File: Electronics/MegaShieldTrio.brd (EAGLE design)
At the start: 99.8 x 80 mm, 40 parts, among them X1 Vehicle control, X2 ODO_JACK, X3 ODO_JACK, X4 RJ45-8L-B, X5 RJ45-8L-B

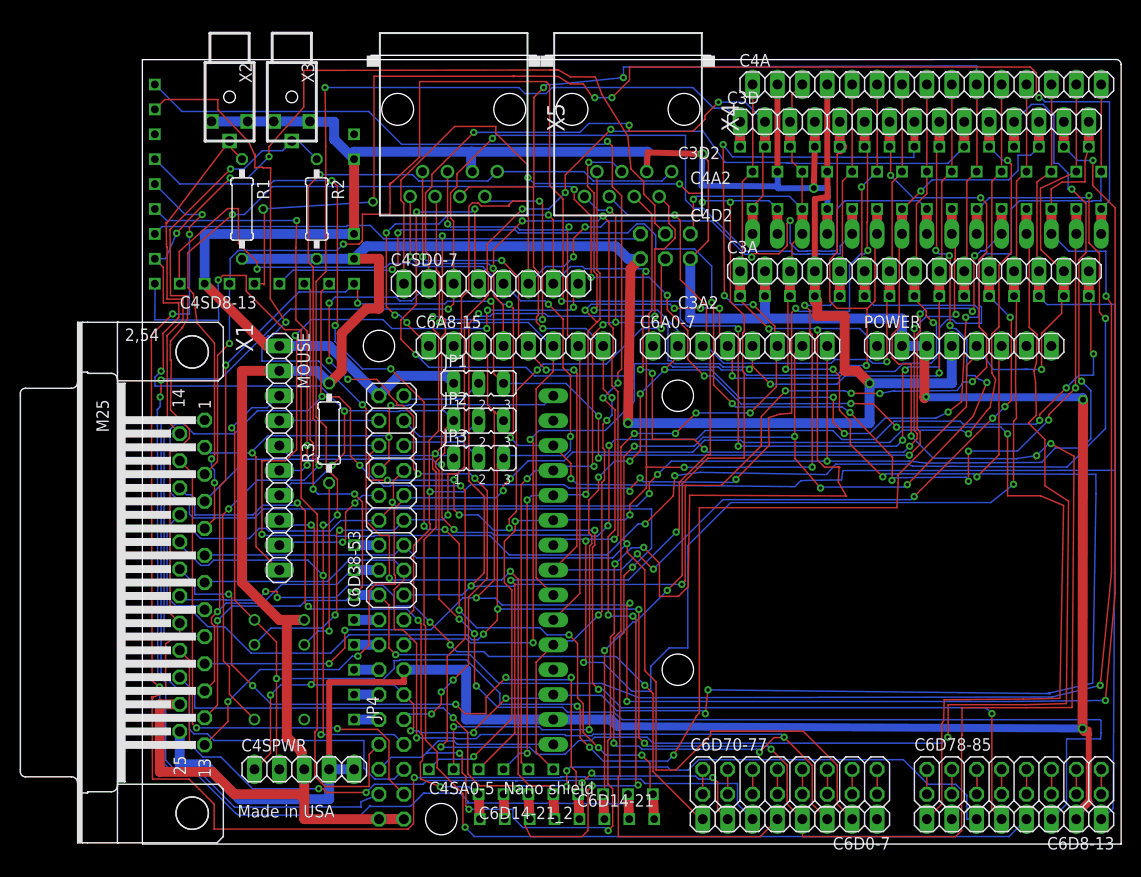
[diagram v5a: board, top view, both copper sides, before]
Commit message: Proto area; thickened traces
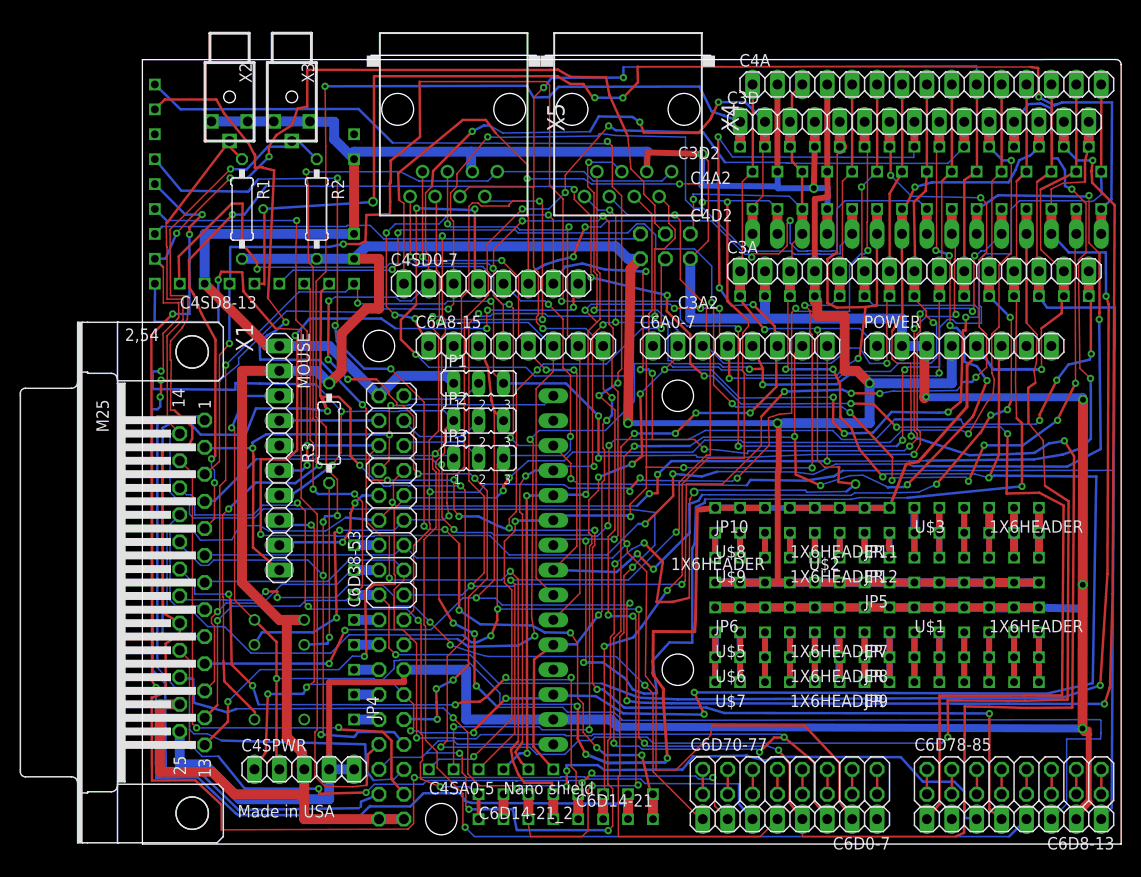
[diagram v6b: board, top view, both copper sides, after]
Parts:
- added JP10, JP11, JP12, JP5, JP6, JP7, JP8, JP9: (no value), Elcano:1X8HEADER
- added U$1, U$2, U$3, U$5, U$6, U$7, U$8, U$9: 1X6HEADER, Elcano:1X6HEADER
- moved C6D14-21 0.13 mm to (52.1, 2.54)
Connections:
- new net N$1: JP11.P$1, JP12.P$1
- new net N$10: JP11.P$3, JP12.P$3, U$3.P$1
- new net N$11: JP11.P$4, JP12.P$4, U$3.P$2
- new net N$12: JP11.P$5, JP12.P$5, U$3.P$3
- new net N$13: JP11.P$6, JP12.P$6, U$3.P$4
- new net N$14: JP11.P$7, JP12.P$7, U$3.P$5
- new net N$15: JP11.P$8, JP12.P$8, U$3.P$6
- new net N$16: U$5.P$1, U$6.P$1, U$7.P$1
- new net N$17: U$5.P$2, U$6.P$2, U$7.P$2
- new net N$18: U$5.P$3, U$6.P$3, U$7.P$3
- new net N$19: U$5.P$4, U$6.P$4, U$7.P$4
- new net N$2: JP11.P$2, JP12.P$2
- new net N$20: U$5.P$5, U$6.P$5, U$7.P$5
- new net N$21: U$5.P$6, U$6.P$6, U$7.P$6
- new net N$22: JP7.P$1, JP8.P$1, JP9.P$1
- new net N$25: JP7.P$2, JP8.P$2, JP9.P$2
- new net N$26: JP7.P$3, JP8.P$3, JP9.P$3
- new net N$27: JP7.P$4, JP8.P$4, JP9.P$4
- new net N$29: JP7.P$5, JP8.P$5, JP9.P$5
- new net N$32: JP7.P$6, JP8.P$6, JP9.P$6
- new net N$33: JP7.P$7, JP8.P$7, JP9.P$7
- new net N$34: JP7.P$8, JP8.P$8, JP9.P$8
- new net N$35: U$8.P$1, U$9.P$1
- new net N$36: U$8.P$2, U$9.P$2
- new net N$40: U$8.P$3, U$9.P$3
- new net N$42: U$8.P$4, U$9.P$4
- new net N$43: U$8.P$5, U$9.P$5
- new net N$51: U$8.P$6, U$9.P$6
- net +5V: now also JP5.P$1, JP5.P$2, JP5.P$3, JP5.P$4, JP5.P$5, JP5.P$6, JP5.P$7, JP5.P$8, U$2.P$1, U$2.P$2, U$2.P$3, U$2.P$4, U$2.P$5, U$2.P$6
- net 3.3V: now also JP10.P$1, JP10.P$2, JP10.P$3, JP10.P$4, JP10.P$5, JP10.P$6, JP10.P$7, JP10.P$8
- net GND: now also JP6.P$1, JP6.P$2, JP6.P$3, JP6.P$4, JP6.P$5, JP6.P$6, JP6.P$7, JP6.P$8, U$1.P$1, U$1.P$2, U$1.P$3, U$1.P$4, U$1.P$5, U$1.P$6
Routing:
- net GND: track 394.0 -> 498.9 mm, vias 5 -> 6
- net +5V: track 253.6 -> 356.4 mm, vias 2 -> 3
- net 3.3V: track 199.4 -> 225.4 mm
- net N$21: track 0.00 -> 12.9 mm
- net N$17: track 0.00 -> 12.7 mm
- net N$16: track 0.00 -> 12.7 mm
- net N$13: track 0.00 -> 12.7 mm
- net N$11: track 0.00 -> 12.7 mm
- net N$34: track 0.00 -> 10.2 mm
- net N$33: track 0.00 -> 10.2 mm
- net N$32: track 0.00 -> 10.2 mm
- net N$29: track 0.00 -> 10.2 mm
- net N$27: track 0.00 -> 10.2 mm
- net N$26: track 0.00 -> 10.2 mm
- net N$25: track 0.00 -> 10.2 mm
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
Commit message: Rear facing sonars; angles adjusted
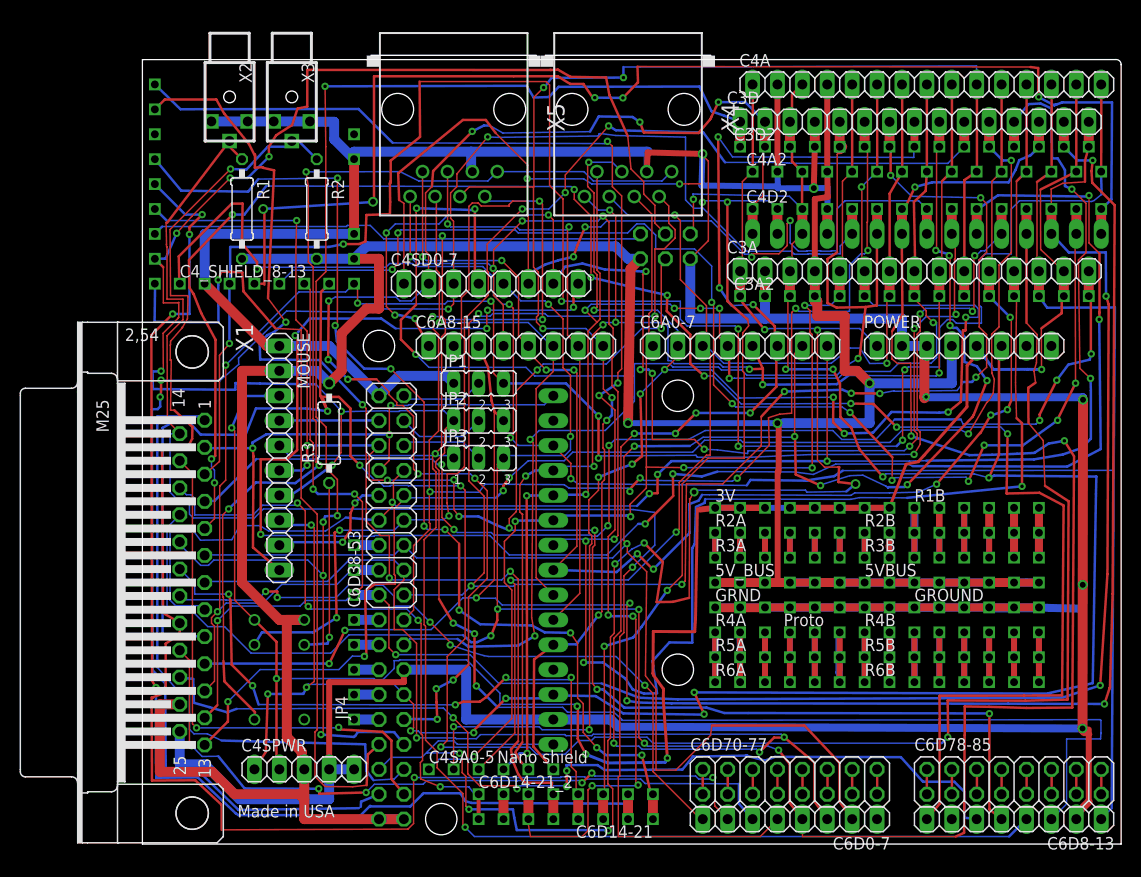
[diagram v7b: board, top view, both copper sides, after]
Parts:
- removed U$2: 1X6HEADER, Elcano:1X6HEADER
- added 5V_BUS: (no value), Elcano:1X6HEADER
- 3V: value (none) -> (none)
- C3A: value C3 Analog -> (none)
- C3A2, C4A2, C4D2: value 1X15HEADER -> (none)
- C4A: value C4 Analog -> (none)
- C4D: value C4 Digital -> (none)
- C4_SHIELD_8-13: value Nano shield -> (none)
- C6A8-15: value C6 Analog In 8-15 -> (none)
- GROUND, R1B, R2A, R3A, R5A, R6A: value 1X6HEADER -> (none)
- JP1: value D52/12 -> (none)
- JP2: value D50/11 -> (none)
- R4A: value 1X6HEADER -> Proto
- X2: value ODO_JACK -> 2odo__
- X3: value ODO_JACK -> 1odo__
- renumbered C4SD8-13 to C4_SHIELD_8-13, JP10 to 3V, JP11 to R2B, JP12 to R3B, JP5 to 5VBUS, JP6 to GRND, JP7 to R4B, JP8 to R5B, JP9 to R6B, U$1 to GROUND, U$3 to R1B, U$4 to INU, U$5 to R4A, U$6 to R5A, U$7 to R6A, U$8 to R2A, U$9 to R3A
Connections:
- net N$27 renamed R5B
- net +5V: now also 5V_BUS.P$1, 5V_BUS.P$2, 5V_BUS.P$3, 5V_BUS.P$4, 5V_BUS.P$5, 5V_BUS.P$6; no longer U$2.P$1, U$2.P$2, U$2.P$3, U$2.P$4, U$2.P$5, U$2.P$6
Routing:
- net +5V: track 356.4 -> 364.1 mm

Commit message: Silkscreens; smaller sonar board
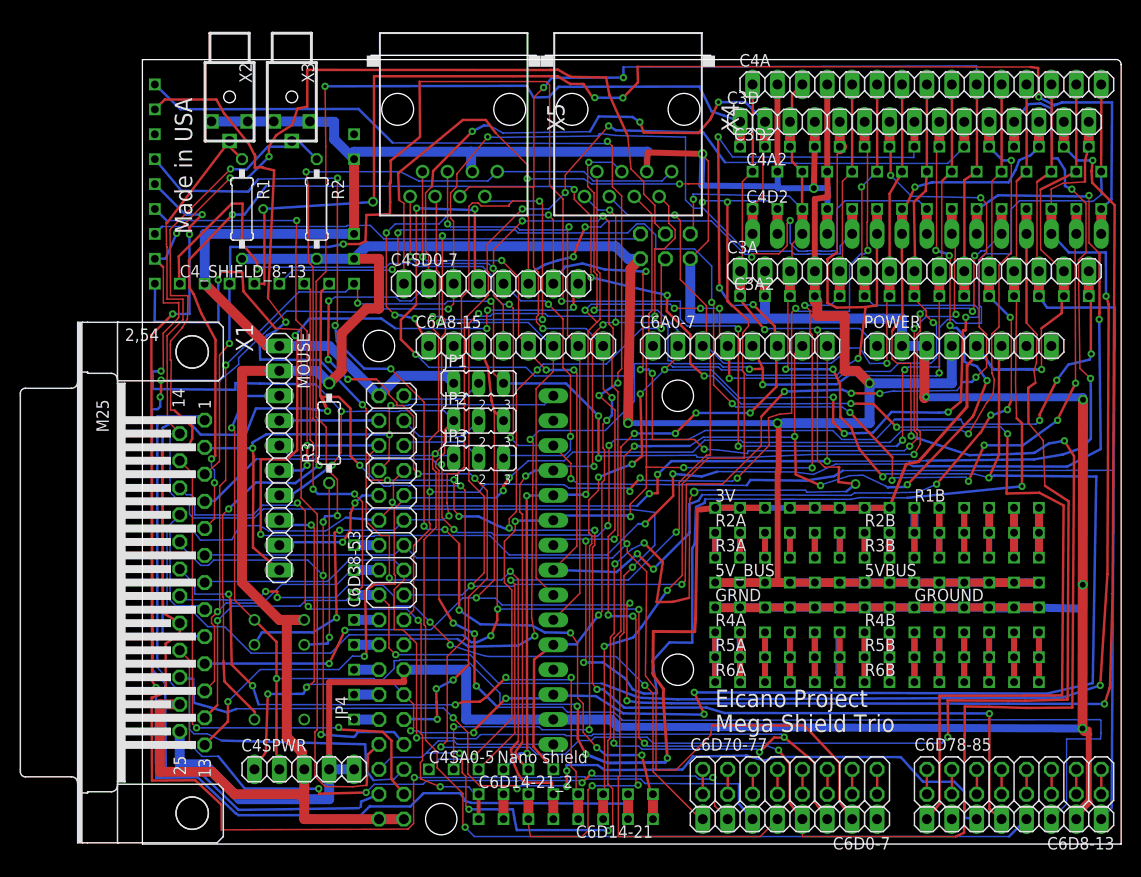
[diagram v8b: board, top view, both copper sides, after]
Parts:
- R4A: value Proto -> (none)
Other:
- board text added: "Elcano Project"
- board text added: "Mega Shield Trio"
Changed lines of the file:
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@@
 <layer number="16" name="Bottom" color="1" fill="1" visible="no" active="yes"/>
 <layer number="17" name="Pads" color="2" fill="1" visible="yes" active="yes"/>
-<layer number="18" name="Vias" color="2" fill="1" visible="no" active="yes"/>
+<layer number="18" name="Vias" color="2" fill="1" visible="yes" active="yes"/>
 <layer number="19" name="Unrouted" color="6" fill="1" visible="yes" active="yes"/>
 <layer number="20" name="Dimension" color="15" fill="1" visible="yes" active="yes"/>
-<layer number="21" name="tPlace" color="7" fill="1" visible="no" active="yes"/>
-<layer number="22" name="bPlace" color="7" fill="1" visible="yes" active="yes"/>
+<layer number="21" name="tPlace" color="7" fill="1" visible="yes" active="yes"/>
+<layer number="22" name="bPlace" color="7" fill="1" visible="no" active="yes"/>
 <layer number="23" name="tOrigins" color="15" fill="1" visible="yes" active="yes"/>
 <layer number="24" name="bOrigins" color="15" fill="1" visible="yes" active="yes"/>
-<layer number="25" name="tNames" color="7" fill="1" visible="no" active="yes"/>
-<layer number="26" name="bNames" color="7" fill="1" visible="yes" active="yes"/>
-<layer number="27" name="tValues" color="7" fill="1" visible="no" active="yes"/>
+<layer number="25" name="tNames" color="7" fill="1" visible="yes" active="yes"/>
+<layer number="26" name="bNames" color="7" fill="1" visible="no" active="yes"/>
+<layer number="27" name="tValues" color="7" fill="1" visible="yes" active="yes"/>
 <layer number="28" name="bValues" color="7" fill="1" visible="no" active="yes"/>
 <layer number="29" name="tStop" color="7" fill="3" visible="no" active="yes"/>
@@
 <wire x1="99.822" y1="79.502" x2="99.314" y2="80.01" width="0" layer="20" curve="90"/>
 <wire x1="99.314" y1="80.01" x2="6.35" y2="80" width="0" layer="20"/>
-<text x="9.7028" y="2.7178" size="1.27" layer="25" font="vector">Made in USA</text>
 <wire x1="0" y1="0" x2="99.822" y2="0" width="0" layer="20"/>
 <wire x1="99.822" y1="0" x2="99.822" y2="79.502" width="0" layer="20"/>
+<text x="58.42" y="13.97" size="1.778" layer="21">Elcano Project</text>
+<text x="58.42" y="11.43" size="1.778" layer="21">Mega Shield Trio</text>
+<text x="5.08" y="62.23" size="1.778" layer="21" rot="R90">Made in USA</text>
 </plain>
 <attributes>
@@
 <element name="R3B" library="Elcano" package="1X8HEADER" value="" x="73.66" y="29.21"/>
 <element name="R1B" library="Elcano" package="1X6HEADER" value=" " x="78.74" y="34.29"/>
-<element name="R4A" library="Elcano" package="1X6HEADER" value="Proto" x="58.42" y="21.59"/>
+<element name="R4A" library="Elcano" package="1X6HEADER" value=" " x="58.42" y="21.59"/>
 <element name="R5A" library="Elcano" package="1X6HEADER" value=" " x="58.42" y="19.05"/>
 <element name="R6A" library="Elcano" package="1X6HEADER" value="" x="58.42" y="16.51"/>
